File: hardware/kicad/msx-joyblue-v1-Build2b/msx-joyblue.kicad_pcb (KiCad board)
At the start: 2 copper layers, 90 x 63 mm, 37 parts, among them J1 MSX Port1, J2 MSX Port2, J4 I2C, SW1 JOY PWR, SW2 MODE, SW3 SWAP, U1 74LS03, U2 74LS03, U3 ESP32 Kit, U4 74LS03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

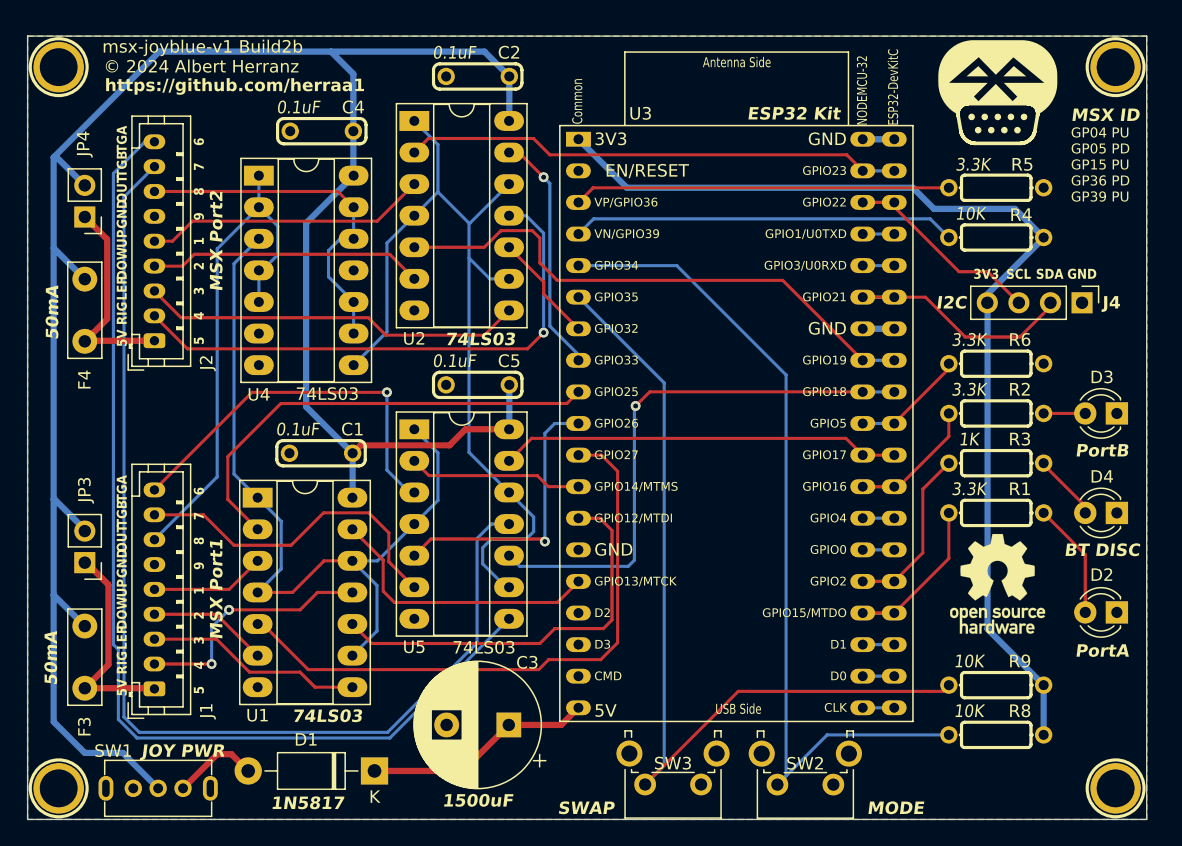
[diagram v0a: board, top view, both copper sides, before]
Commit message: hardware: add missing pull-ups to v1 Build2b
Signed-off-by: Albert Herranz <albert_herranz@yahoo.es>
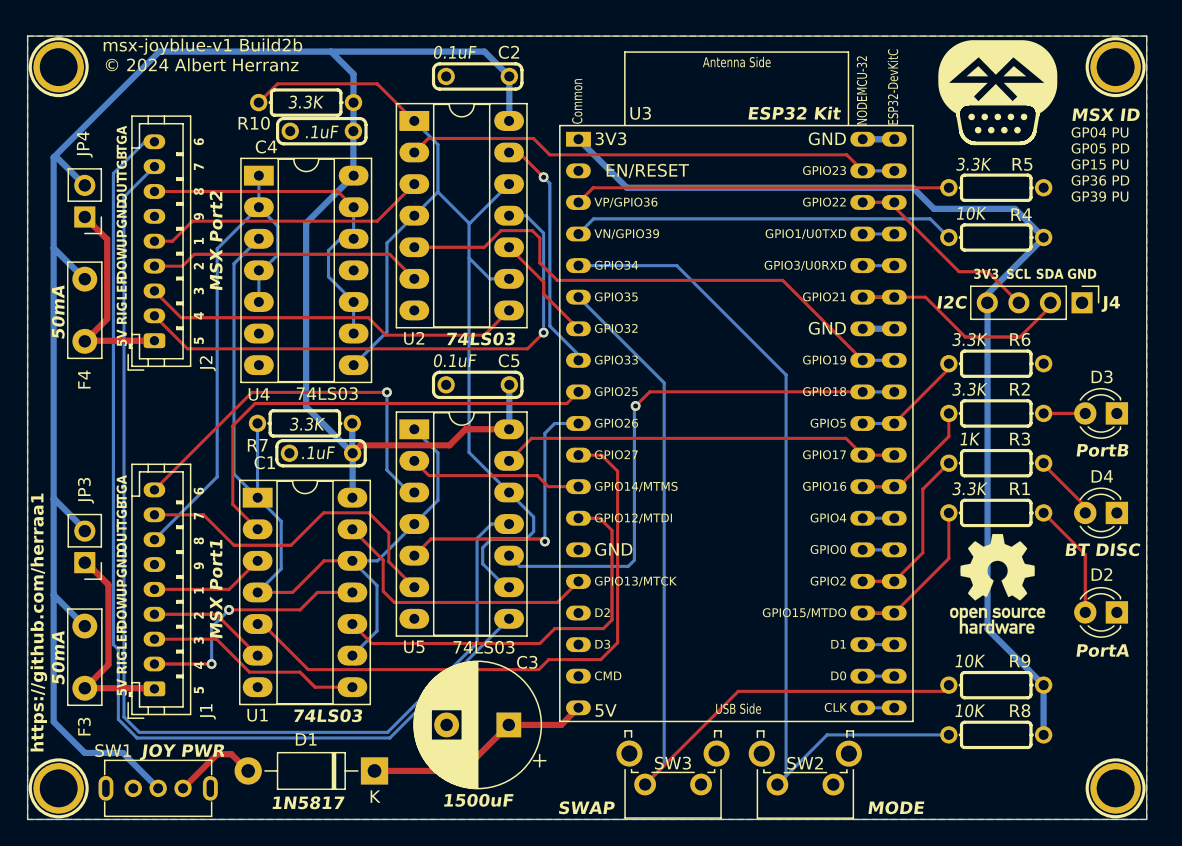
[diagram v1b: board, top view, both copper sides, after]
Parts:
- added R10: 3.3K, My_Components:Res_762, F.Cu at (121.6, 79.8)
- added R7: 3.3K, My_Components:Res_762, F.Cu at (121.5, 105.6)
- C1, C4: value 0.1uF -> .1uF
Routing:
- net /~{J2_OUT_1}: track 70.8 -> 85.1 mm
- net /~{J1_OUT_1}: track 65.0 -> 70.9 mm
- net /JOY_5V: track 171.2 -> 173.6 mm
- net GPIO_J1_UP: track 37.2 -> 38.1 mm
